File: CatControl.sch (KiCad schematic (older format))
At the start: 4 parts

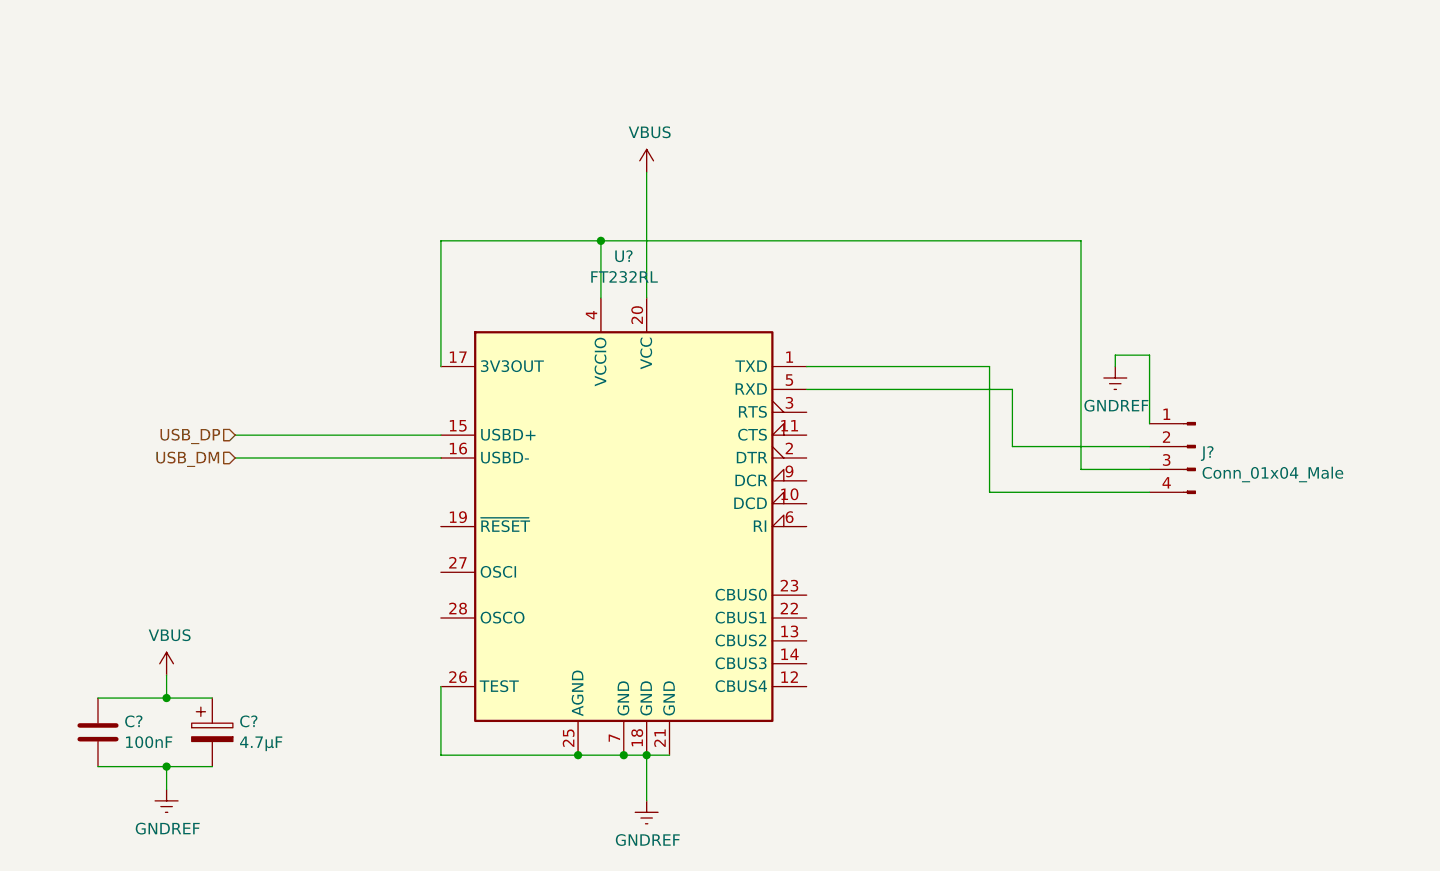
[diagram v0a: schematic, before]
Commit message: Moved clock to its own page
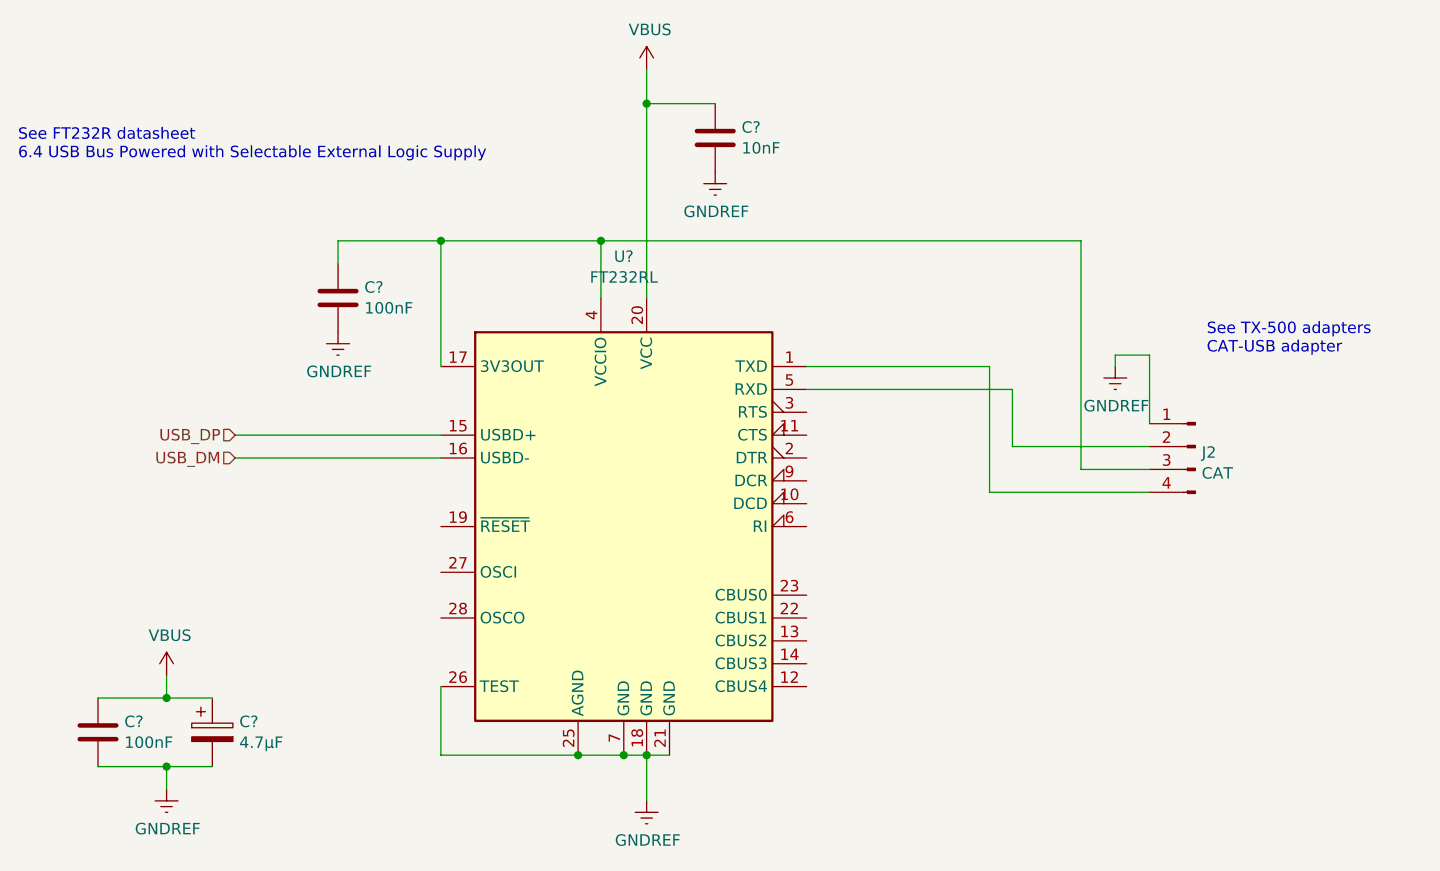
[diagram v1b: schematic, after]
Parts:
- added C?: 10nF, symbol Device:C
- added C?: 100nF, symbol Device:C
- J2: renamed from J?; value Conn_01x04_Male -> CAT
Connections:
- net GNDREF: now also C?.2, C?.2
- net VBUS: now also C?.1
- net at J2.3 (Pin_3), U?.17 (3V3OUT), U?.4 (VCCIO): now also C?.1
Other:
- note added: "See FT232R datasheet\n6.4 USB Bus Powered with Selectable External Logic Supply"
- note added: "See TX-500 adapters\nCAT-USB adapter"
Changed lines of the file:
@@
 $Descr A4 11693 8268
 encoding utf-8
-Sheet 3 5
+Sheet 3 6
 Title ""
 Date ""
@@
 P 7950 3250
 AR Path="/605A84FC" Ref="J?"  Part="1"
-AR Path="/6059C0E9/605A84FC" Ref="J?"  Part="1"
-F 0 "J?" H 7922 3224 50  0000 R CNN
-F 1 "Conn_01x04_Male" H 7922 3133 50  0000 R CNN
+AR Path="/6059C0E9/605A84FC" Ref="J2"  Part="1"
+F 0 "J2" H 7922 3224 50  0000 R CNN
+F 1 "CAT" H 7922 3133 50  0000 R CNN
 F 2 "" H 7950 3250 50  0001 C CNN
 F 3 "~" H 7950 3250 50  0001 C CNN
@@
 L power:VBUS #PWR?
 U 1 1 605C5EC8
-P 5550 2050
-F 0 "#PWR?" H 5550 1900 50  0001 C CNN
-F 1 "VBUS" H 5565 2223 50  0000 C CNN
-F 2 "" H 5550 2050 50  0001 C CNN
-F 3 "" H 5550 2050 50  0001 C CNN
-	1    5550 2050
-	1    0    0    -1
-$EndComp
-Wire Wire Line
-	5550 2050 5550 2600
+P 5550 1600
+F 0 "#PWR?" H 5550 1450 50  0001 C CNN
+F 1 "VBUS" H 5565 1773 50  0000 C CNN
+F 2 "" H 5550 1600 50  0001 C CNN
+F 3 "" H 5550 1600 50  0001 C CNN
+	1    5550 1600
+	1    0    0    -1
+$EndComp
 Wire Wire Line
 	5350 2350 5350 2600
@@
 Wire Wire Line
 	3450 4650 3650 4650
+Text Notes 2800 2000 0    50   ~ 0
+See FT232R datasheet\n6.4 USB Bus Powered with Selectable External Logic Supply
+Text Notes 8000 2850 0    50   ~ 0
+See TX-500 adapters\nCAT-USB adapter
+$Comp
+L Device:C C?
+U 1 1 604C7383
+P 5850 1900
+F 0 "C?" H 5965 1946 50  0000 L CNN
+F 1 "10nF" H 5965 1855 50  0000 L CNN
+F 2 "" H 5888 1750 50  0001 C CNN
+F 3 "~" H 5850 1900 50  0001 C CNN
+	1    5850 1900
+	1    0    0    -1
+$EndComp
+$Comp
+L power:GNDREF #PWR?
+U 1 1 604C84F9
+P 5850 2050
+F 0 "#PWR?" H 5850 1800 50  0001 C CNN
+F 1 "GNDREF" H 5855 1877 50  0000 C CNN
+F 2 "" H 5850 2050 50  0001 C CNN
+F 3 "" H 5850 2050 50  0001 C CNN
+	1    5850 2050
+	1    0    0    -1
+$EndComp
+Wire Wire Line
+	5550 1600 5550 1750
+Wire Wire Line
+	5850 1750 5550 1750
+Connection ~ 5550 1750
+Wire Wire Line
+	5550 1750 5550 2600
+$Comp
+L Device:C C?
+U 1 1 604CE119
+P 4200 2600
+F 0 "C?" H 4315 2646 50  0000 L CNN
+F 1 "100nF" H 4315 2555 50  0000 L CNN
+F 2 "" H 4238 2450 50  0001 C CNN
+F 3 "~" H 4200 2600 50  0001 C CNN
+	1    4200 2600
+	1    0    0    -1
+$EndComp
+$Comp
+L power:GNDREF #PWR?
+U 1 1 604CEB86
+P 4200 2750
+F 0 "#PWR?" H 4200 2500 50  0001 C CNN
+F 1 "GNDREF" H 4205 2577 50  0000 C CNN
+F 2 "" H 4200 2750 50  0001 C CNN
+F 3 "" H 4200 2750 50  0001 C CNN
+	1    4200 2750
+	1    0    0    -1
+$EndComp
+Wire Wire Line
+	4650 2350 4200 2350
+Wire Wire Line
+	4200 2350 4200 2450
+Connection ~ 4650 2350
 $EndSCHEMATC

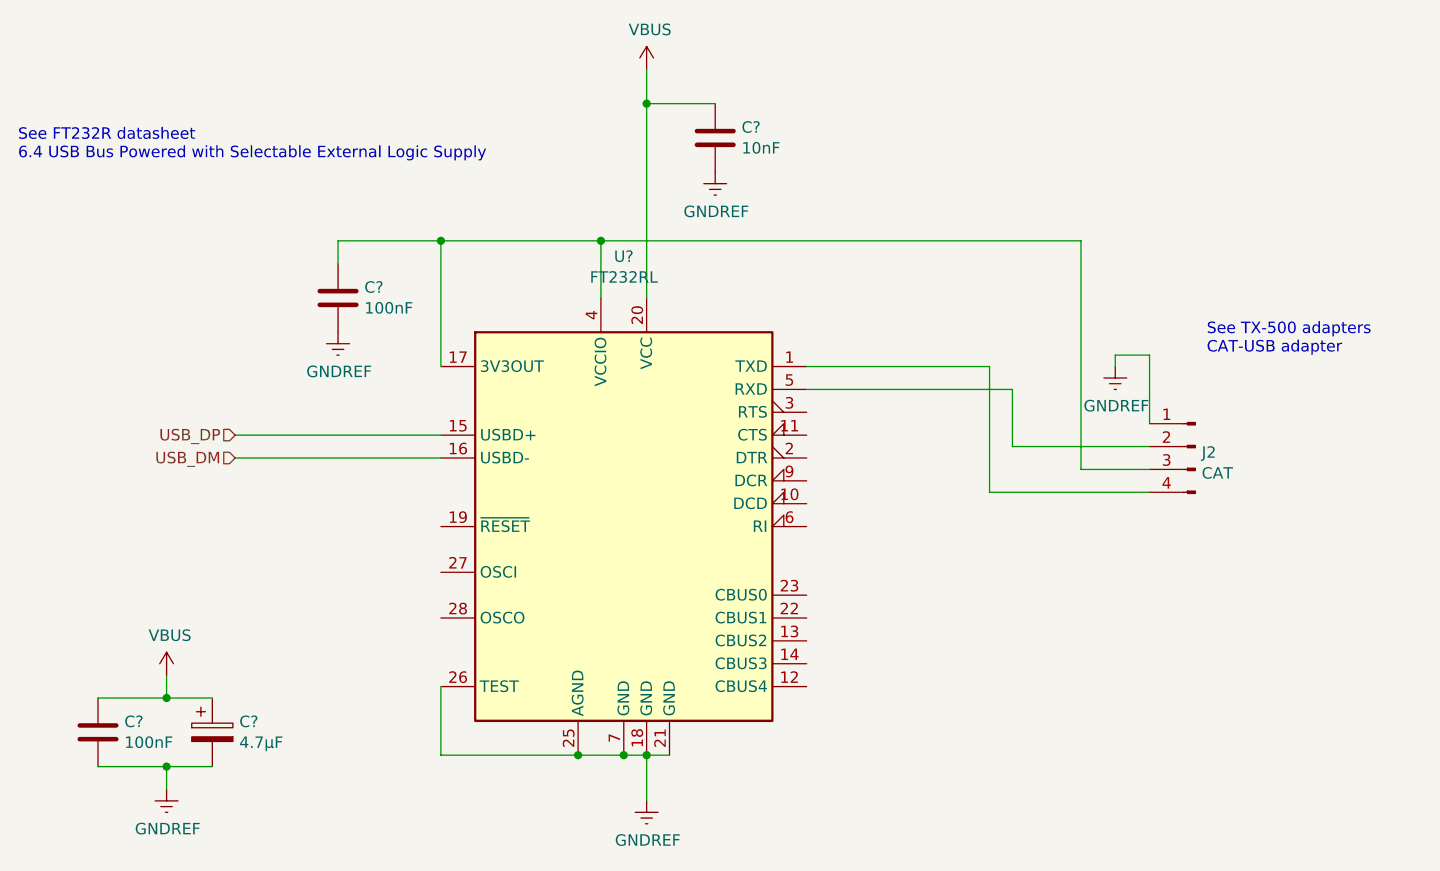
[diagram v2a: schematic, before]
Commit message: First pass at pcb layout
Not really ready to set that in stone, but wanted to get an idea of what size enclosure will work.
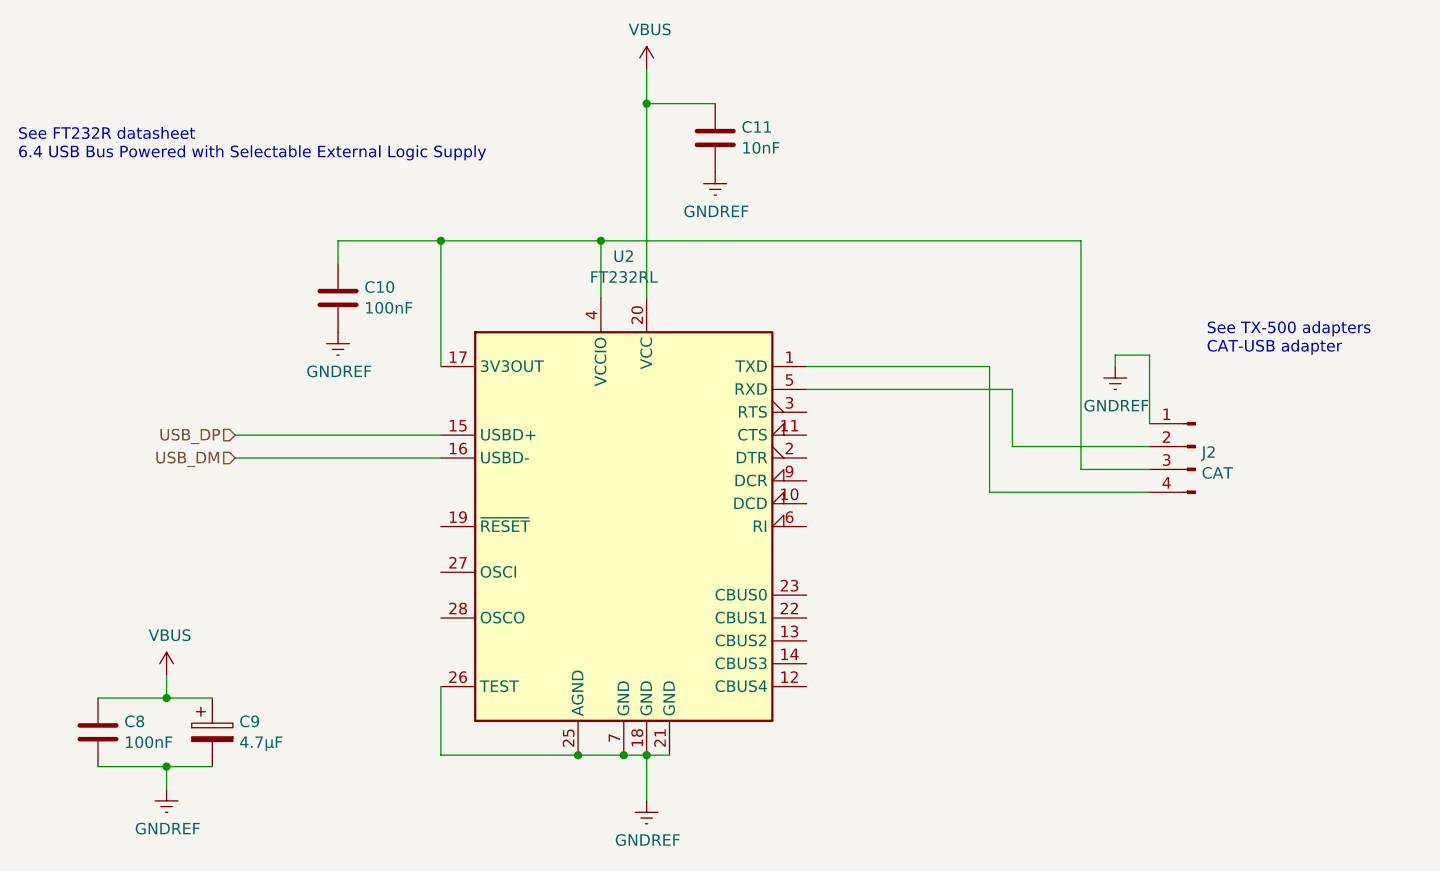
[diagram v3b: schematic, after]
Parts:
- C10, C11, C8: renamed from C?; footprint (none) -> Capacitor_SMD:C_1210_3225Metric
- C9: renamed from C?; footprint (none) -> Capacitor_SMD:CP_Elec_4x3
- J2: footprint (none) -> Connector_JST:JST_PH_B4B-PH-SM4-TB_1x04-1MP_P2.00mm_Vertical
- gave numbers to parts that had none: 1
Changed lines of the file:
@@
 P 5450 3600
 AR Path="/605A84F6" Ref="U?"  Part="1"
-AR Path="/6059C0E9/605A84F6" Ref="U?"  Part="1"
-F 0 "U?" H 5450 4781 50  0000 C CNN
+AR Path="/6059C0E9/605A84F6" Ref="U2"  Part="1"
+F 0 "U2" H 5450 4781 50  0000 C CNN
 F 1 "FT232RL" H 5450 4690 50  0000 C CNN
 F 2 "Package_SO:SSOP-28_5.3x10.2mm_P0.65mm" H 6550 2700 50  0001 C CNN
@@
 F 0 "J2" H 7922 3224 50  0000 R CNN
 F 1 "CAT" H 7922 3133 50  0000 R CNN
-F 2 "" H 7950 3250 50  0001 C CNN
+F 2 "Connector_JST:JST_PH_B4B-PH-SM4-TB_1x04-1MP_P2.00mm_Vertical" H 7950 3250 50  0001 C CNN
 F 3 "~" H 7950 3250 50  0001 C CNN
 	1    7950 3250
@@
 	4650 3200 3750 3200
 $Comp
-L power:GNDREF #PWR?
+L power:GNDREF #PWR0118
 U 1 1 605BF8D4
 P 5550 4800
-F 0 "#PWR?" H 5550 4550 50  0001 C CNN
+F 0 "#PWR0118" H 5550 4550 50  0001 C CNN
 F 1 "GNDREF" H 5555 4627 50  0000 C CNN
 F 2 "" H 5550 4800 50  0001 C CNN
@@
 	7600 2850 7600 2900
 $Comp
-L power:GNDREF #PWR?
+L power:GNDREF #PWR0119
 U 1 1 605C410A
 P 7600 2900
-F 0 "#PWR?" H 7600 2650 50  0001 C CNN
+F 0 "#PWR0119" H 7600 2650 50  0001 C CNN
 F 1 "GNDREF" H 7605 2727 50  0000 C CNN
 F 2 "" H 7600 2900 50  0001 C CNN
@@
 Connection ~ 5450 4600
 $Comp
-L power:VBUS #PWR?
+L power:VBUS #PWR0120
 U 1 1 605C5EC8
 P 5550 1600
-F 0 "#PWR?" H 5550 1450 50  0001 C CNN
+F 0 "#PWR0120" H 5550 1450 50  0001 C CNN
 F 1 "VBUS" H 5565 1773 50  0000 C CNN
 F 2 "" H 5550 1600 50  0001 C CNN
@@
 	5350 2350 7450 2350
 $Comp
-L power:VBUS #PWR?
+L power:VBUS #PWR0121
 U 1 1 605C93BD
 P 3450 4250
-F 0 "#PWR?" H 3450 4100 50  0001 C CNN
+F 0 "#PWR0121" H 3450 4100 50  0001 C CNN
 F 1 "VBUS" H 3465 4423 50  0000 C CNN
 F 2 "" H 3450 4250 50  0001 C CNN
@@
 $EndComp
 $Comp
-L power:GNDREF #PWR?
+L power:GNDREF #PWR0122
 U 1 1 605C99BA
 P 3450 4750
-F 0 "#PWR?" H 3450 4500 50  0001 C CNN
+F 0 "#PWR0122" H 3450 4500 50  0001 C CNN
 F 1 "GNDREF" H 3455 4577 50  0000 C CNN
 F 2 "" H 3450 4750 50  0001 C CNN
@@
 $EndComp
 $Comp
-L Device:C C?
+L Device:C C8
 U 1 1 605CA219
 P 3150 4500
-F 0 "C?" H 3265 4546 50  0000 L CNN
+F 0 "C8" H 3265 4546 50  0000 L CNN
 F 1 "100nF" H 3265 4455 50  0000 L CNN
-F 2 "" H 3188 4350 50  0001 C CNN
+F 2 "Capacitor_SMD:C_1210_3225Metric" H 3188 4350 50  0001 C CNN
 F 3 "~" H 3150 4500 50  0001 C CNN
 	1    3150 4500
@@
 $EndComp
 $Comp
-L Device:CP C?
+L Device:CP C9
 U 1 1 605CB7E6
 P 3650 4500
-F 0 "C?" H 3768 4546 50  0000 L CNN
+F 0 "C9" H 3768 4546 50  0000 L CNN
 F 1 "4.7μF" H 3768 4455 50  0000 L CNN
-F 2 "" H 3688 4350 50  0001 C CNN
+F 2 "Capacitor_SMD:CP_Elec_4x3" H 3688 4350 50  0001 C CNN
 F 3 "~" H 3650 4500 50  0001 C CNN
 	1    3650 4500
@@
 See TX-500 adapters\nCAT-USB adapter
 $Comp
-L Device:C C?
+L Device:C C11
 U 1 1 604C7383
 P 5850 1900
-F 0 "C?" H 5965 1946 50  0000 L CNN
+F 0 "C11" H 5965 1946 50  0000 L CNN
 F 1 "10nF" H 5965 1855 50  0000 L CNN
-F 2 "" H 5888 1750 50  0001 C CNN
+F 2 "Capacitor_SMD:C_1210_3225Metric" H 5888 1750 50  0001 C CNN
 F 3 "~" H 5850 1900 50  0001 C CNN
 	1    5850 1900
@@
 $EndComp
 $Comp
-L power:GNDREF #PWR?
+L power:GNDREF #PWR0123
 U 1 1 604C84F9
 P 5850 2050
-F 0 "#PWR?" H 5850 1800 50  0001 C CNN
+F 0 "#PWR0123" H 5850 1800 50  0001 C CNN
 F 1 "GNDREF" H 5855 1877 50  0000 C CNN
 F 2 "" H 5850 2050 50  0001 C CNN
@@
 	5550 1750 5550 2600
 $Comp
-L Device:C C?
+L Device:C C10
 U 1 1 604CE119
 P 4200 2600
-F 0 "C?" H 4315 2646 50  0000 L CNN
+F 0 "C10" H 4315 2646 50  0000 L CNN
 F 1 "100nF" H 4315 2555 50  0000 L CNN
-F 2 "" H 4238 2450 50  0001 C CNN
+F 2 "Capacitor_SMD:C_1210_3225Metric" H 4238 2450 50  0001 C CNN
 F 3 "~" H 4200 2600 50  0001 C CNN
 	1    4200 2600
@@
 $EndComp
 $Comp
-L power:GNDREF #PWR?
+L power:GNDREF #PWR0124
 U 1 1 604CEB86
 P 4200 2750
-F 0 "#PWR?" H 4200 2500 50  0001 C CNN
+F 0 "#PWR0124" H 4200 2500 50  0001 C CNN
 F 1 "GNDREF" H 4205 2577 50  0000 C CNN
 F 2 "" H 4200 2750 50  0001 C CNN
